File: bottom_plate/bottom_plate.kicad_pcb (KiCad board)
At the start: 2 copper layers, 323.6 x 142.9 mm, 143 parts, among them SW1 SW_Push, SW11 SW_Push, SW12 SW_Push, SW13 SW_Push, SW14 SW_Push, SW15 SW_Push, SW16 SW_Push, SW17 SW_Push, SW18 SW_Push, SW19 SW_Push, SW2 SW_Push, SW20 SW_Push, SW21 SW_Push, SW22 SW_Push, SW23 SW_Push, SW24 SW_Push, SW25 SW_Push, SW26 SW_Push, SW27 SW_Push, SW28 SW_Push, SW29 SW_Push, SW3 SW_Push, SW30 SW_Push, SW31 SW_Push, SW32 SW_Push, SW33 SW_Push, SW34 SW_Push, SW35 SW_Push, SW36 SW_Push, SW37 SW_Push, SW38 SW_Push, SW39 SW_Push, SW4 SW_Push, SW40 SW_Push, SW41 SW_Push, SW42 SW_Push, SW43 SW_Push, SW44 SW_Push, SW45 SW_Push, SW46 SW_Push, SW47 SW_Push, SW48 SW_Push, SW49 SW_Push, SW5 SW_Push, SW50 SW_Push, SW51 SW_Push, SW52 SW_Push, SW53 SW_Push, SW54 SW_Push, SW55 SW_Push, SW56 SW_Push, SW57 SW_Push, SW58 SW_Push, SW59 SW_Push, SW6 SW_Push, SW60 SW_Push, SW61 SW_Push, SW7 SW_Push, SW8 SW_Push, SW9 SW_Push

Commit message: Plates and covers
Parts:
- removed D1, D10, D11, D12, D13, D14, D15, D16, D17, D18, D19, D2, D20, D21, D22, D23, D24, D25, D26, D27, D28, D29, D3, D30, D31, D32, D33, D34, D35, D36, D37, D38, D39, D4, D40, D41, D42, D43, D44, D45, D46, D47, D48, D49, D5, D50, D51, D52, D53, D54, D55, D56, D57, D58, D59, D6, D60, D61, D7, D8, D9: 1N4148, footprints:diode_TH_SMD
- ENC2: value EVQWGD001 -> Switch Hole; footprint footprints:EVQWGD001 -> footprints:Switch_Hole
- SW1, SW11, SW12, SW13, SW14, SW15, SW16, SW17, SW18, SW19, SW2, SW20, SW21, SW22, SW23, SW24, SW25, SW26, SW27, SW28, SW29, SW3, SW30, SW31, SW32, SW33, SW34, SW35, SW36, SW37, SW38, SW39, SW4, SW40, SW41, SW42, SW43, SW44, SW45, SW46, SW47, SW48, SW49, SW5, SW50, SW51, SW52, SW53, SW54, SW55, SW56, SW57, SW58, SW59, SW6, SW60, SW61, SW7, SW8, SW9: footprint footprints:Kailh_socket_PG1350_optional -> footprints:Switch_Hole
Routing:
- net (no net): track 1079.4 -> 0.00 mm

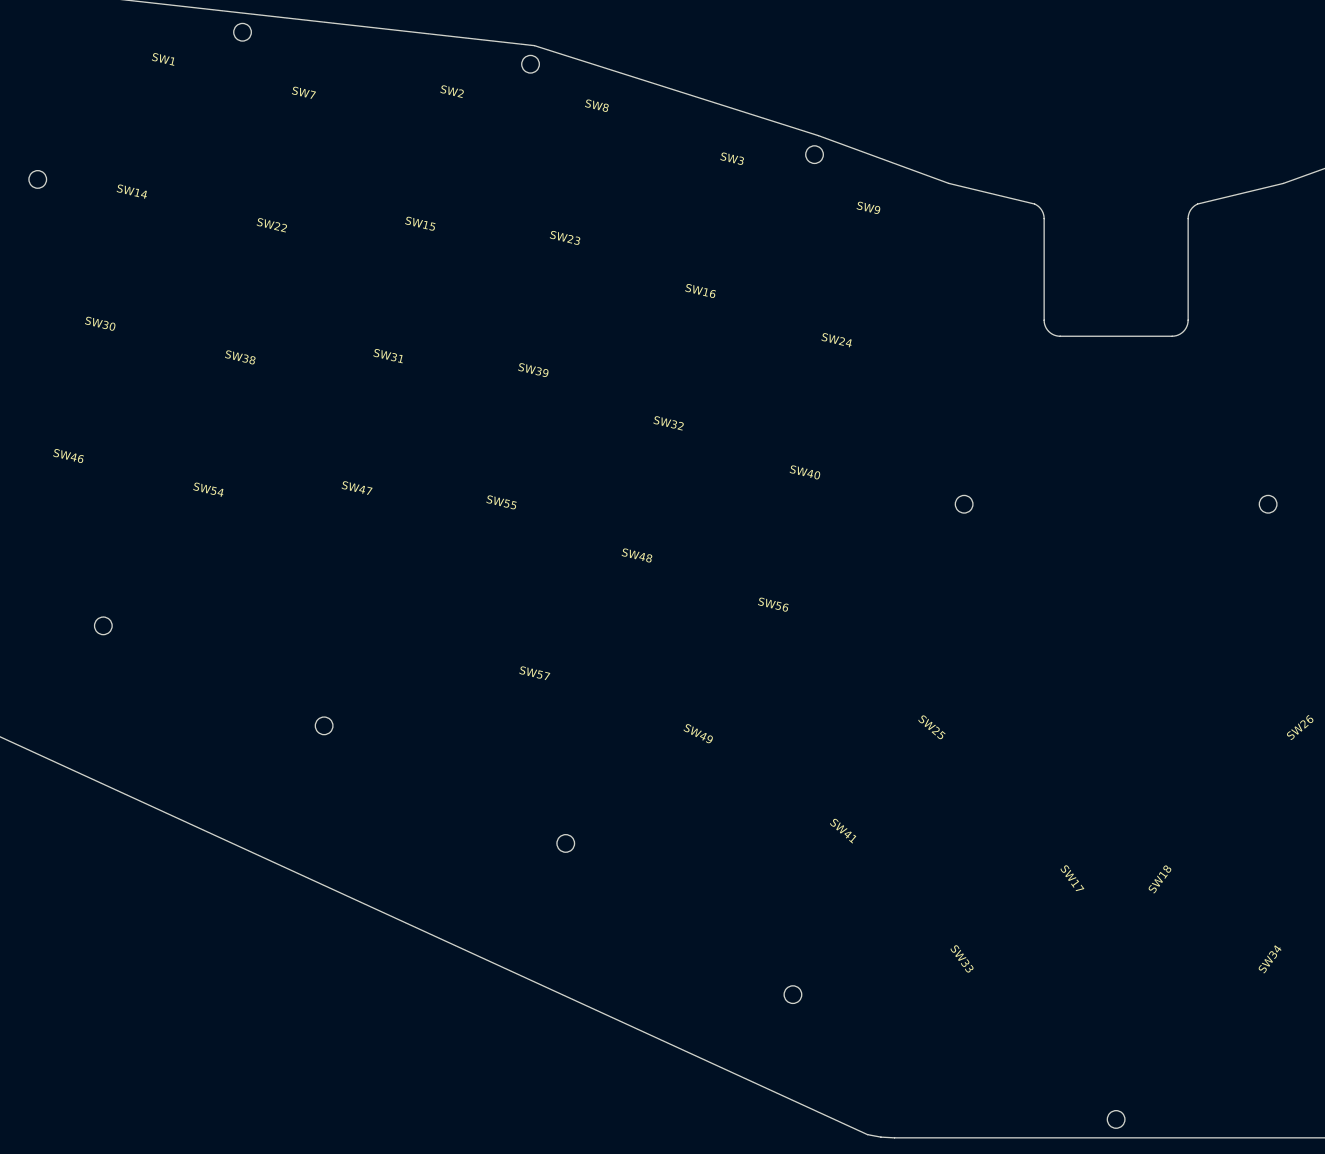
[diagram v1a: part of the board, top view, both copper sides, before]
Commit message: Moving mounting holes
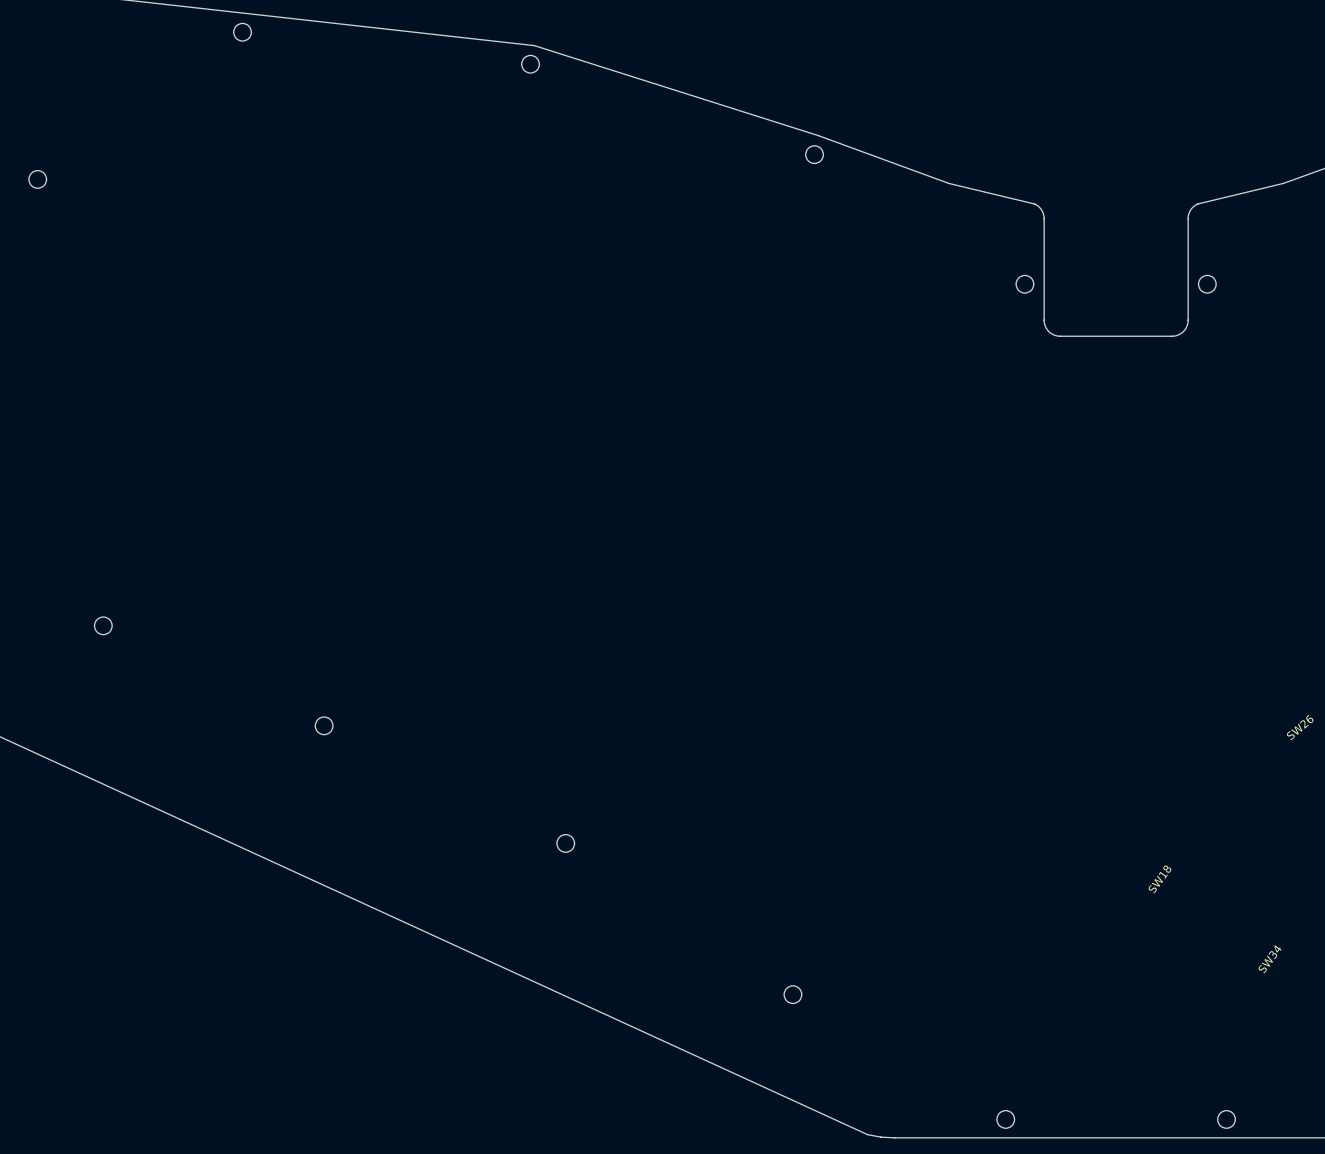
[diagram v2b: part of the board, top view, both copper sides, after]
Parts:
- added H23: MountingHole, MountingHole:MountingHole_2.2mm_M2, F.Cu at (13.8, 79.9)
- moved H6 28.5 mm to (-11.4, -24.5)
- moved H10 28.5 mm to (11.4, -24.5)
- moved H1 13.8 mm to (-13.8, 79.9)

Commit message: Done with mounting holes, I guess.
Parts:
- removed the H12 at (-109.2, -56.0)
- removed H15, H19, H23, H5, H7: MountingHole, MountingHole:MountingHole_2.2mm_M2
- removed the H16 at (-134.8, -37.6)
- removed the H17 at (-40.4, 64.3)
- removed the H20 at (-37.7, -40.7)
- removed the H3 at (-126.6, 18.2)
- removed the H8 at (-73.2, -52.0)
- added H12: MountingHole, MountingHole:MountingHole_2.2mm_M2, F.Cu at (146.1, -58.1)
- added H12: MountingHole, MountingHole:MountingHole_2.2mm_M2, F.Cu at (-146.1, -58.1)
- added H12: MountingHole, MountingHole:MountingHole_2.2mm_M2, F.Cu at (-99.7, -54.8)
- added H16: MountingHole, MountingHole:MountingHole_2.2mm_M2, F.Cu at (159.2, -17.9)
- added H16: MountingHole, MountingHole:MountingHole_2.2mm_M2, F.Cu at (-159.2, -17.9)
- added H16: MountingHole, MountingHole:MountingHole_2.2mm_M2, F.Cu at (-138.6, -21.0)
- added H17: MountingHole, MountingHole:MountingHole_2.2mm_M2, F.Cu at (-56.6, 67.2)
- added H17: MountingHole, MountingHole:MountingHole_2.2mm_M2, F.Cu at (101.6, 46.5)
- added H17: MountingHole, MountingHole:MountingHole_2.2mm_M2, F.Cu at (56.6, 67.2)
- added H17: MountingHole, MountingHole:MountingHole_2.2mm_M2, F.Cu at (-101.6, 46.5)
- added H20: MountingHole, MountingHole:MountingHole_2.2mm_M2, F.Cu at (11.5, -26.1)
- added H20: MountingHole, MountingHole:MountingHole_2.2mm_M2, F.Cu at (-11.5, -26.1)
- added H20: MountingHole, MountingHole:MountingHole_2.2mm_M2, F.Cu at (-46.9, -43.5)
- added H3: MountingHole, MountingHole:MountingHole_2.2mm_M2, F.Cu at (144.1, 27.1)
- added H3: MountingHole, MountingHole:MountingHole_2.2mm_M2, F.Cu at (-144.1, 27.1)
- added H3: MountingHole, MountingHole:MountingHole_2.2mm_M2, F.Cu at (-126.7, 18.0)
- added H8: MountingHole, MountingHole:MountingHole_2.2mm_M2, F.Cu at (73.2, -51.9)
- added H8: MountingHole, MountingHole:MountingHole_2.2mm_M2, F.Cu at (-73.2, -51.9)
- moved H9 110.4 mm to (-0.00, 79.6), turned to 180 degrees
- moved H21 75.7 mm to (22.6, 4.30)
- moved H10 63.2 mm to (0.00, 37.7)
- moved H6 30.9 mm to (-22.6, 4.30)
- moved H1 22.4 mm to (-34.6, 71.7)
- moved H18 9.62 mm to (46.9, -43.5)
- moved H22 9.58 mm to (99.7, -54.8)
- moved H2 9.40 mm to (34.6, 71.7)
- moved H4 9.15 mm to (77.6, 42.9)
- moved H13 9.15 mm to (-77.6, 42.9)
- moved H11 0.22 mm to (126.7, 18.0)
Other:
- outline, holes or cut-outs redrawn

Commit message: Gerbers for bottom plate
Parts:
- removed ENC2: Switch Hole, footprints:Switch_Hole
- removed the H12 at (146.1, -58.1)
- removed the H12 at (-146.1, -58.1)
- removed the H12 at (-99.7, -54.8)
- removed the H16 at (159.2, -17.9)
- removed the H16 at (-159.2, -17.9)
- removed the H16 at (-138.6, -21.0)
- removed H17 (x4), H8 (x2), H9: MountingHole, MountingHole:MountingHole_2.2mm_M2
- removed the H20 at (11.5, -26.1)
- removed the H20 at (-11.5, -26.1)
- removed the H20 at (-46.9, -43.5)
- removed the H3 at (144.1, 27.1)
- removed the H3 at (-144.1, 27.1)
- removed the H3 at (-126.7, 18.0)
- removed SW1, SW11, SW12, SW13, SW14, SW15, SW16, SW17, SW18, SW19, SW2, SW20, SW21, SW22, SW23, SW24, SW25, SW26, SW27, SW28, SW29, SW3, SW30, SW31, SW32, SW33, SW34, SW35, SW36, SW37, SW38, SW39, SW4, SW40, SW41, SW42, SW43, SW44, SW45, SW46, SW47, SW48, SW49, SW5, SW50, SW51, SW52, SW53, SW54, SW55, SW56, SW57, SW58, SW59, SW6, SW60, SW61, SW7, SW8, SW9: SW_Push, footprints:Switch_Hole
- added H12: MountingHole, MountingHole:MountingHole_2.2mm_M2, F.Cu at (-142.7, -64.2)
- added H15: MountingHole, MountingHole:MountingHole_2.2mm_M2, F.Cu at (168.2, -26.2)
- added H16: MountingHole, MountingHole:MountingHole_2.2mm_M2, F.Cu at (-168.2, -26.2)
- added H20: MountingHole, MountingHole:MountingHole_2.2mm_M2, F.Cu at (-78.8, -57.8)
- added H3: MountingHole, MountingHole:MountingHole_2.2mm_M2, F.Cu at (-142.7, 26.1)
- moved H22 44.0 mm to (142.7, -64.2)
- moved H6 42.7 mm to (-15.4, -37.8)
- moved H21 42.7 mm to (15.4, -37.8)
- moved H10 42.0 mm to (0.00, 79.7)
- moved H18 35.0 mm to (78.8, -57.8)
- moved H4 19.7 mm to (96.4, 48.8)
- moved H13 19.7 mm to (-96.4, 48.8)
- moved H11 17.9 mm to (142.7, 26.1), turned to 357 degrees
- moved H2 17.6 mm to (52.2, 70.5)
- moved H1 17.6 mm to (-52.2, 70.5)
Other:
- board size 323.6 x 142.9 mm -> 341.3 x 148.9 mm
